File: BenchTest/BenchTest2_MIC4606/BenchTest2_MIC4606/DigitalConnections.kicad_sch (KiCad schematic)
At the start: 64 parts, among them J8 Conn_01x10, U13 SRV05-4, U14 SRV05-4

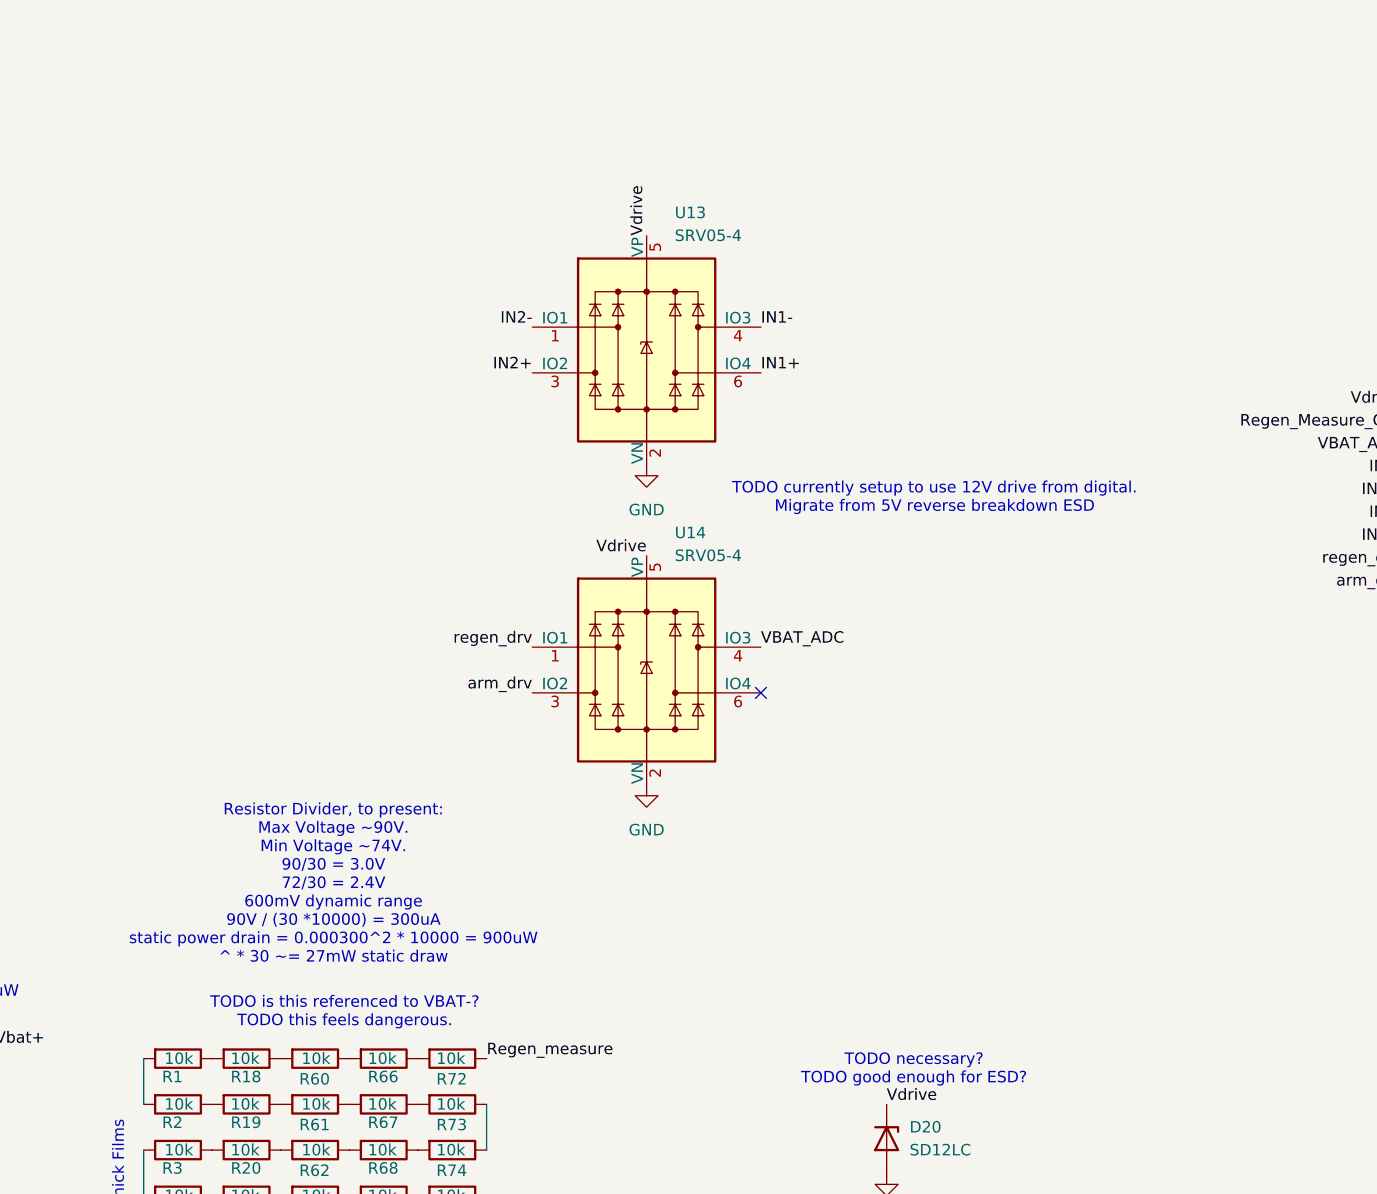
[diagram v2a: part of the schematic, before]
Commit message: Migrated to 5V drive from digital side
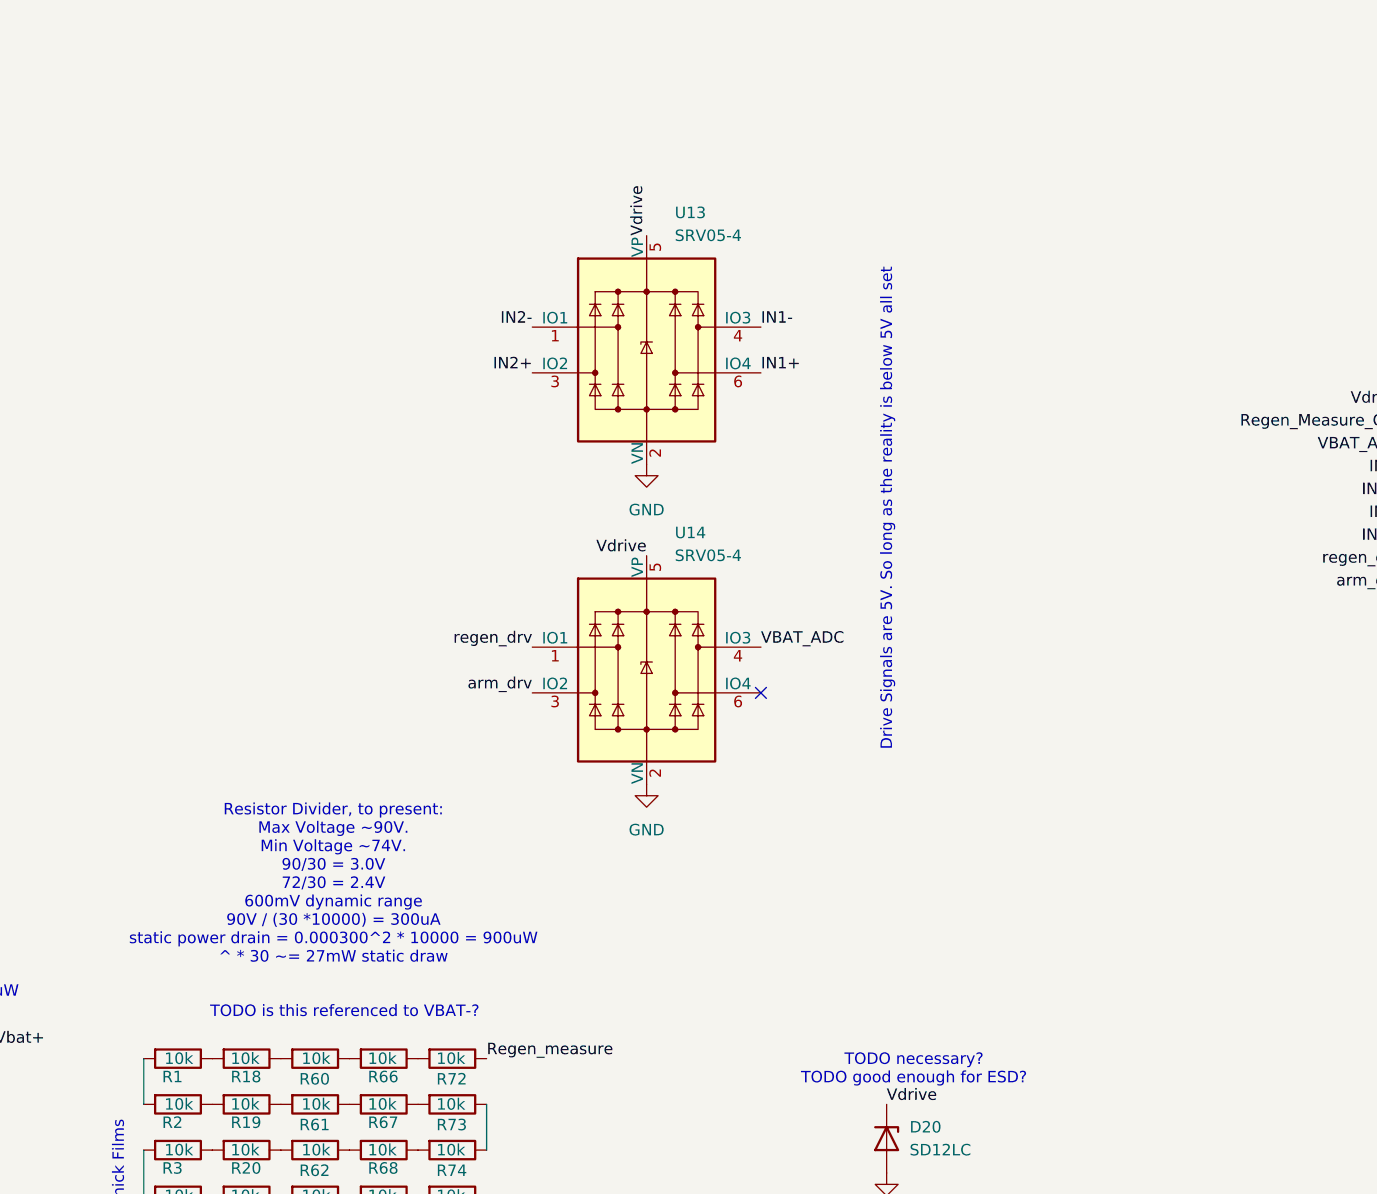
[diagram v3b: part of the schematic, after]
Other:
- note added: "Drive Signals are 5V. So long as the reality is below 5V all set"
- note added: "TODO is this referenced to VBAT-?"
- note removed: "TODO currently setup to use 12V drive from digital. Migrate from 5V reverse breakdown ESD"
- note removed: "TODO is this referenced to VBAT-? TODO this feels dangerous."
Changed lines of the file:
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@@
 	(generator_version "9.0")
 	(paper "A4")
-	(text "TODO is this referenced to VBAT-?\nTODO this feels dangerous. "
+	(text "TODO is this referenced to VBAT-?"
 		(exclude_from_sim no)
 		(at 98.552 153.67 0)
@@
 		)
 	)
-	(text "TODO currently setup to use 12V drive from digital. \nMigrate from 5V reverse breakdown ESD"
+	(text "Drive Signals are 5V. So long as the reality is below 5V all set"
 		(exclude_from_sim no)
-		(at 164.084 96.52 0)
+		(at 158.75 97.79 90)
 		(effects
 			(font

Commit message: Footprint / Capacitor Assignment
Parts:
- D20: footprint (none) -> Diode_SMD:D_SOD-323_HandSoldering
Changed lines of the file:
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@@
 			)
 		)
-		(property "Footprint" ""
+		(property "Footprint" "Diode_SMD:D_SOD-323_HandSoldering"
 			(at 158.75 167.64 0)
 			(effects
